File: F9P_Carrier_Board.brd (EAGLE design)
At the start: 56.9 x 66 mm, 148 parts, among them J4 U.FL, J5 QWIIC_RIGHT_ANGLE, J6 MICROMOD-2222-C, J8 JTAG, U1 U-BLOX_ZED-F9P, U5 AP7361C-33

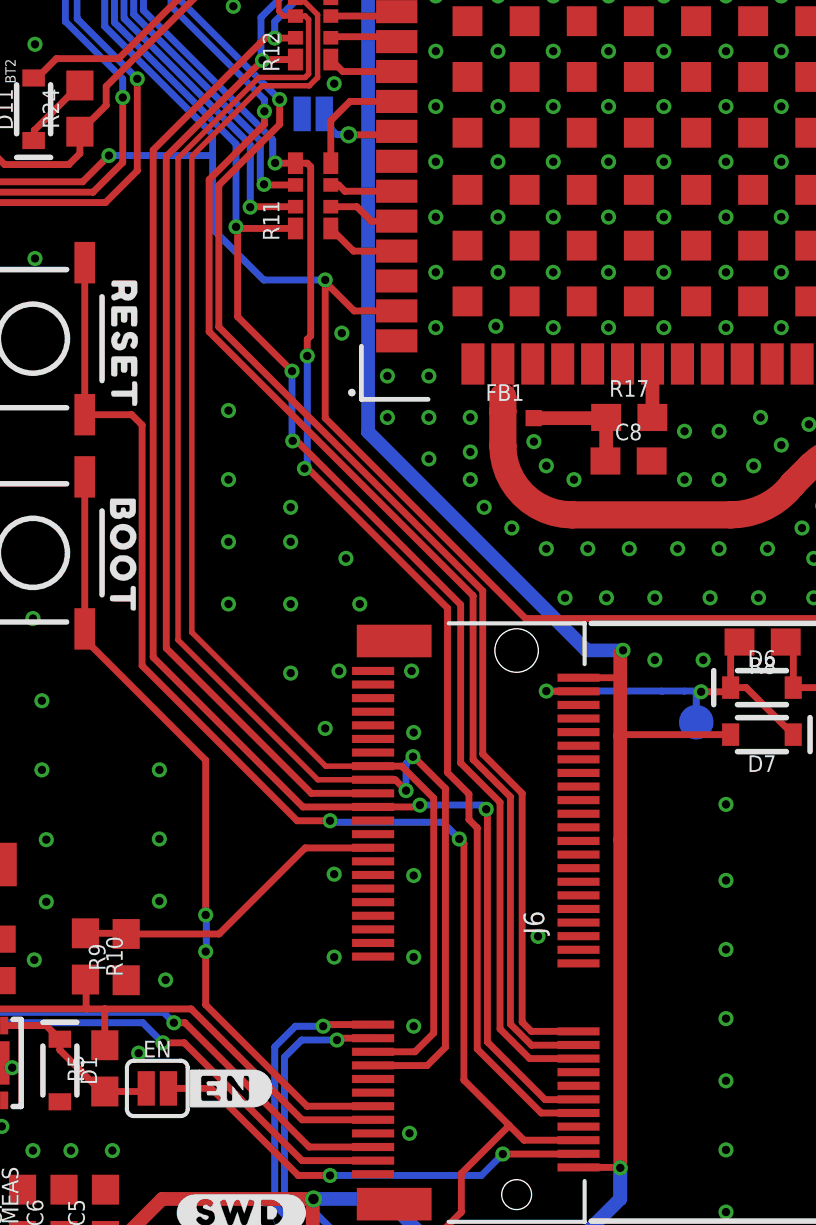
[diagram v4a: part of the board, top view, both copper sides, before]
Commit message: Removes "INT" trace to MicroMod connector
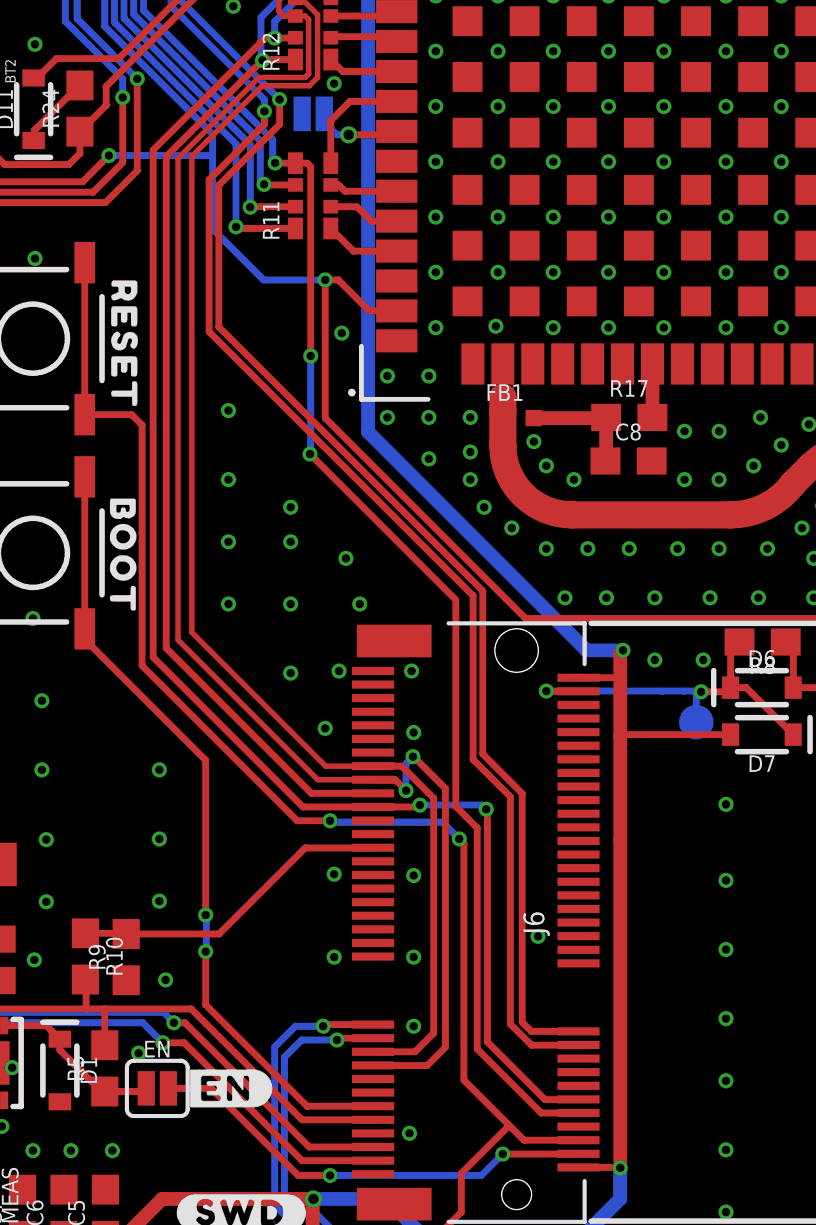
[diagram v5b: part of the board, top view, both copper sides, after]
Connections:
- net INT: no longer J6.18
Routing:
- net INT: track 67.1 -> 30.3 mm, vias 3 -> 1
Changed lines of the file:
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@@
 <wire x1="15.4432" y1="58.2168" x2="9.398" y2="64.262" width="0.254" layer="16"/>
 <contactref element="R11" pad="P8"/>
-<contactref element="J6" pad="18"/>
 <wire x1="22.0961" y1="41.008" x2="19.9706" y2="41.008" width="0.254" layer="1"/>
 <wire x1="19.9706" y1="41.008" x2="19.9125" y2="41.0661" width="0.254" layer="1"/>
-<wire x1="32.501" y1="10.494" x2="30.7048" y2="10.494" width="0.254" layer="1"/>
-<wire x1="30.7048" y1="10.494" x2="29.6164" y2="11.5824" width="0.254" layer="1"/>
-<wire x1="29.6164" y1="11.5824" x2="29.6164" y2="19.9136" width="0.254" layer="1"/>
-<wire x1="29.6164" y1="19.9136" x2="28.1686" y2="21.3614" width="0.254" layer="1"/>
-<wire x1="28.1686" y1="21.3614" x2="28.1686" y2="27.178" width="0.254" layer="1"/>
-<wire x1="28.1686" y1="27.178" x2="22.1488" y2="33.1978" width="0.254" layer="1"/>
-<wire x1="22.1488" y1="33.1978" x2="21.9964" y2="33.1978" width="0.254" layer="1"/>
-<via x="21.9964" y="33.1978" extent="1-16" drill="0.3048"/>
-<wire x1="21.9964" y1="33.1978" x2="21.971" y2="33.2232" width="0.254" layer="16"/>
-<wire x1="21.971" y1="33.2232" x2="21.971" y2="35.7632" width="0.254" layer="16"/>
-<via x="21.971" y="35.7632" extent="1-16" drill="0.3048"/>
-<wire x1="21.971" y1="35.7632" x2="19.9706" y2="37.7636" width="0.254" layer="1"/>
-<wire x1="19.9706" y1="37.7636" x2="19.9706" y2="41.008" width="0.254" layer="1"/>
 </signal>
 <signal name="SDA/!CS!">
@@
 <wire x1="21.3552" y1="43.408" x2="21.3476" y2="43.4156" width="0.254" layer="1"/>
 <wire x1="32.501" y1="8.494" x2="31.13" y2="8.494" width="0.254" layer="1"/>
-<wire x1="28.7782" y1="18.9738" x2="28.4734" y2="19.2786" width="0.254" layer="1"/>
-<wire x1="28.4734" y1="20.2184" x2="27.686" y2="21.0058" width="0.254" layer="1"/>
+<wire x1="28.7782" y1="18.9738" x2="27.9908" y2="19.7612" width="0.254" layer="1"/>
 <wire x1="31.13" y1="8.494" x2="28.7782" y2="10.8458" width="0.254" layer="1"/>
 <wire x1="28.7782" y1="10.8458" x2="28.7782" y2="18.9738" width="0.254" layer="1"/>
-<wire x1="28.4734" y1="19.2786" x2="28.4734" y2="20.2184" width="0.254" layer="1"/>
-<wire x1="27.686" y1="21.0058" x2="27.686" y2="27.051" width="0.254" layer="1"/>
-<wire x1="27.686" y1="27.051" x2="22.5552" y2="32.1818" width="0.254" layer="1"/>
-<wire x1="22.4282" y1="32.1818" x2="22.5552" y2="32.1818" width="0.254" layer="1"/>
-<via x="22.4282" y="32.1818" extent="1-16" drill="0.3048"/>
-<wire x1="22.4282" y1="32.1818" x2="22.5298" y2="32.2834" width="0.254" layer="16"/>
-<wire x1="22.5298" y1="32.2834" x2="22.5298" y2="36.322" width="0.254" layer="16"/>
-<via x="22.5298" y="36.322" extent="1-16" drill="0.3048"/>
+<wire x1="27.9908" y1="19.7612" x2="27.9908" y2="27.3558" width="0.254" layer="1"/>
+<wire x1="27.9908" y1="27.3558" x2="22.6314" y2="32.7152" width="0.254" layer="1"/>
+<via x="22.6314" y="32.7152" extent="1-16" drill="0.3048"/>
+<wire x1="22.6314" y1="32.7152" x2="22.6568" y2="32.7406" width="0.254" layer="16"/>
+<wire x1="22.6568" y1="32.7406" x2="22.6568" y2="36.322" width="0.254" layer="16"/>
+<via x="22.6568" y="36.322" extent="1-16" drill="0.3048"/>
 <wire x1="22.0961" y1="43.408" x2="22.5279" y2="43.408" width="0.254" layer="1"/>
 <wire x1="22.6568" y1="43.2791" x2="22.5279" y2="43.408" width="0.254" layer="1"/>
-<wire x1="22.6568" y1="37.0586" x2="22.6568" y2="43.2791" width="0.254" layer="1"/>
-<wire x1="22.5298" y1="36.322" x2="22.5298" y2="36.9316" width="0.254" layer="1"/>
-<wire x1="22.5298" y1="36.9316" x2="22.6568" y2="37.0586" width="0.254" layer="1"/>
+<wire x1="22.6568" y1="36.322" x2="22.6568" y2="43.2791" width="0.254" layer="1"/>
 </signal>
 <signal name="!SAFEBOOT!">
@@
 <contactref element="U1" pad="53"/>
 <contactref element="J10" pad="1"/>
-<wire x1="25.82" y1="37.977" x2="24.253" y2="37.977" width="0.254" layer="1"/>
-<wire x1="23.1902" y1="39.0398" x2="23.1902" y2="39.116" width="0.254" layer="1"/>
+<wire x1="25.82" y1="37.977" x2="24.8118" y2="37.977" width="0.254" layer="1"/>
 <via x="23.1902" y="39.116" extent="1-16" drill="0.3048"/>
 <wire x1="23.1902" y1="39.116" x2="20.9296" y2="39.116" width="0.254" layer="16"/>
@@
 <wire x1="8.128" y1="62.484" x2="6.35" y2="64.262" width="0.254" layer="16"/>
 <wire x1="15.0876" y1="48.4328" x2="15.0876" y2="57.8866" width="0.254" layer="16"/>
-<wire x1="24.253" y1="37.977" x2="23.1902" y2="39.0398" width="0.254" layer="1"/>
+<wire x1="24.8118" y1="37.977" x2="23.6728" y2="39.116" width="0.254" layer="1"/>
+<wire x1="23.1902" y1="39.116" x2="23.6728" y2="39.116" width="0.254" layer="1"/>
 <wire x1="20.9296" y1="39.116" x2="19.05" y2="40.9956" width="0.254" layer="16"/>
 <wire x1="19.05" y1="40.9956" x2="19.05" y2="43.688" width="0.254" layer="16"/>

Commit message: Adds micromod silk to the board, fixes zed reset silk
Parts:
- added U$61: (no value), bot:##ZED_RESET##9
- added U$62: (no value), top:##ZED_RESET##14
- added U$63: (no value), SparkFun-Aesthetics:SFE_LOGO_FLAME_.3
- U$1: device top:##RESET##11 -> top:##SFBOOT##13
- U$2: device top:##SFBOOT##10 -> bot:##SFBOOT##8
- U$25: device bot:##SFBOOT##8 -> SparkFun-MicroMod:MICROMOD_LOGO_.5
- U$41: device bot:##RESET##9 -> SparkFun-MicroMod:MICROMOD_MI_LOGO_1
- moved LOGO3 51.2 mm to (49.1, 1.78)
- moved U$41 39.1 mm to (12.7, 21.6), turned to 0 degrees
- moved U$25 37.3 mm to (40.6, 36.8), flipped to the bottom, turned to 0 degrees
- moved U$1 2.62 mm to (11.4, 60.1)
- moved D4 1.14 mm to (9.14, 54.9)
- moved R15 0.76 mm to (12.2, 54.2)
- moved R16 0.76 mm to (12.2, 55.5)
- flipped U$2 to the top, turned to 270 degrees
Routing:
- net N$12: track 6.14 -> 5.02 mm
- net N$13: track 6.98 -> 5.88 mm
- net ZED_USB_P: track 19.8 -> 20.6 mm
- net ZED_USB_N: track 20.5 -> 21.3 mm
- net GND: track 9.57 -> 8.94 mm
